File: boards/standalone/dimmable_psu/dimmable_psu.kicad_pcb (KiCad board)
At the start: 2 copper layers, 85 x 50 mm, 85 parts, among them J1 DIM_IN, J2 PWM_IN, J3 POWER, J4 POWER_OUT, Q1 2N7002, Q2 IRF540N, Q3 IRF540N, SW1 SW_DIP_SPLIT_x02, U1 LM324, U2 AP2205-ADJ, U3 MAX17651, U4 LMC7660, U5 TPS92640

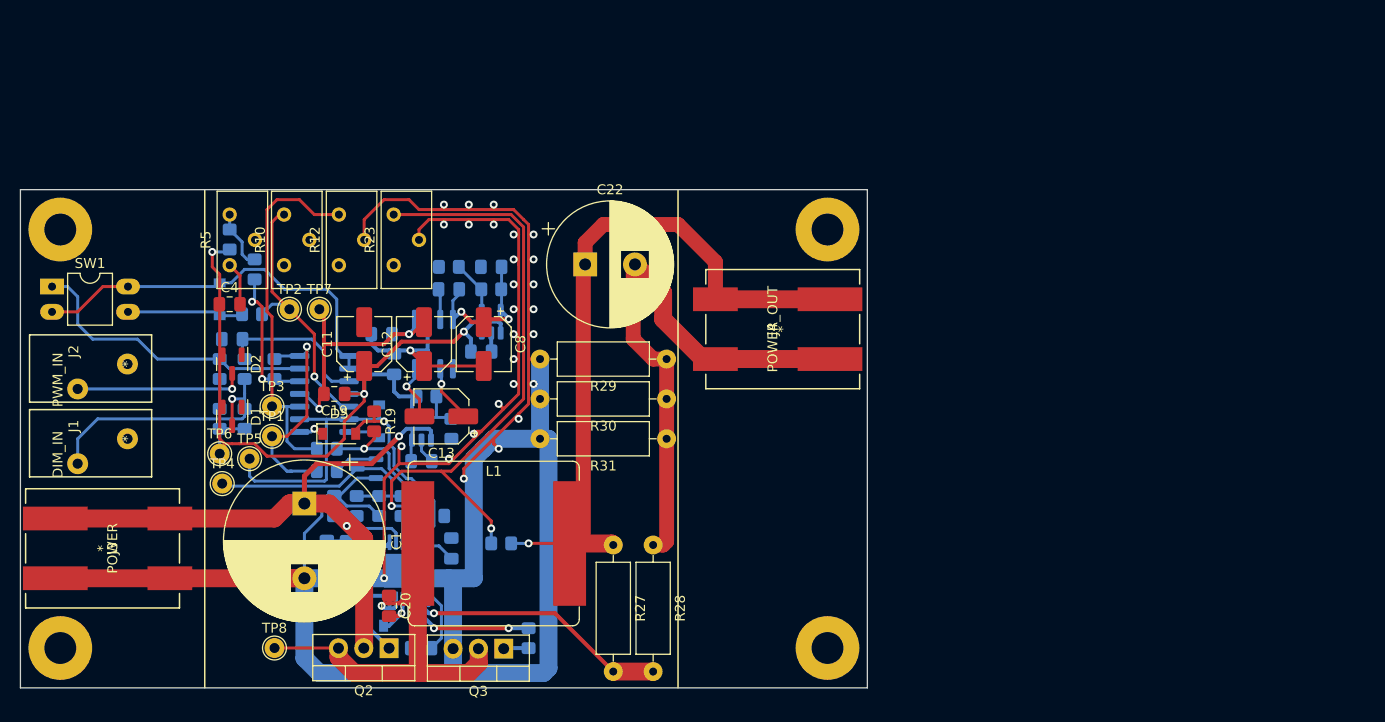
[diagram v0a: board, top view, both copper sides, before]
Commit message: add filled areas and make some cosmetic fixes
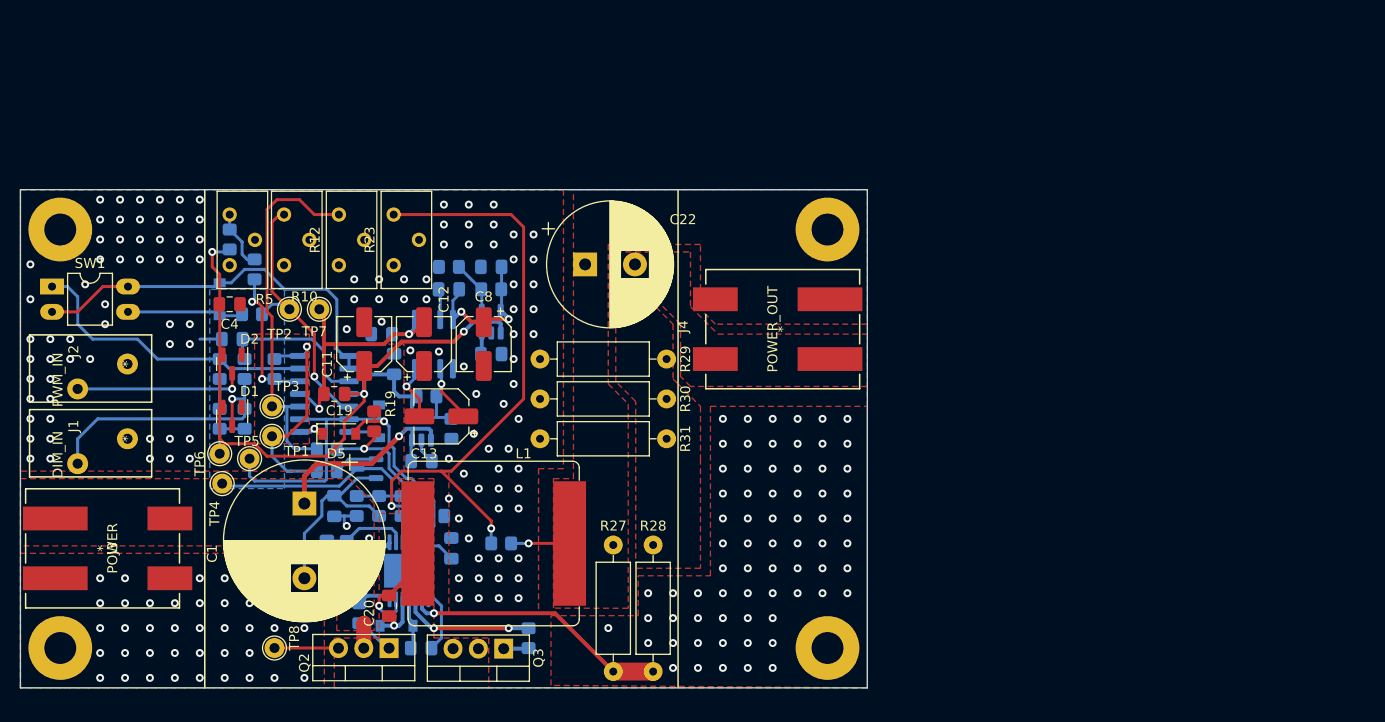
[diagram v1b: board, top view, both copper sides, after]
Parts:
- moved C6 1.03 mm to (47.2, 16.5)
- moved R25 0.50 mm to (34.0, 42.5)
- moved D6 0.35 mm to (37.8, 43.8)
- moved R11 0.05 mm to (30.8, 26.1)
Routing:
- net GND: track 316.9 -> 33.2 mm, vias 28 -> 228
- net /OUT+: track 71.8 -> 6.50 mm
- net /OUT-: track 56.6 -> 0.00 mm
- net VPP: track 75.6 -> 35.0 mm
- net /POWER_JUN: track 49.1 -> 18.1 mm
- net Net-(C20-Pad2): track 5.37 -> 6.43 mm
- net Net-(Q2-Pad1): track 3.54 -> 4.05 mm
- net Net-(R25-Pad1): track 2.91 -> 3.41 mm
- added copper zone on F.Cu, net /OUT+
- added copper zone on F.Cu, net /OUT-
- added copper zone on F.Cu, net /POWER_JUN
- added copper zone on B.Cu, net GND
- added copper zone on F.Cu, net GND
- added copper zone on F.Cu, net VPP

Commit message: replace LDOs with npns
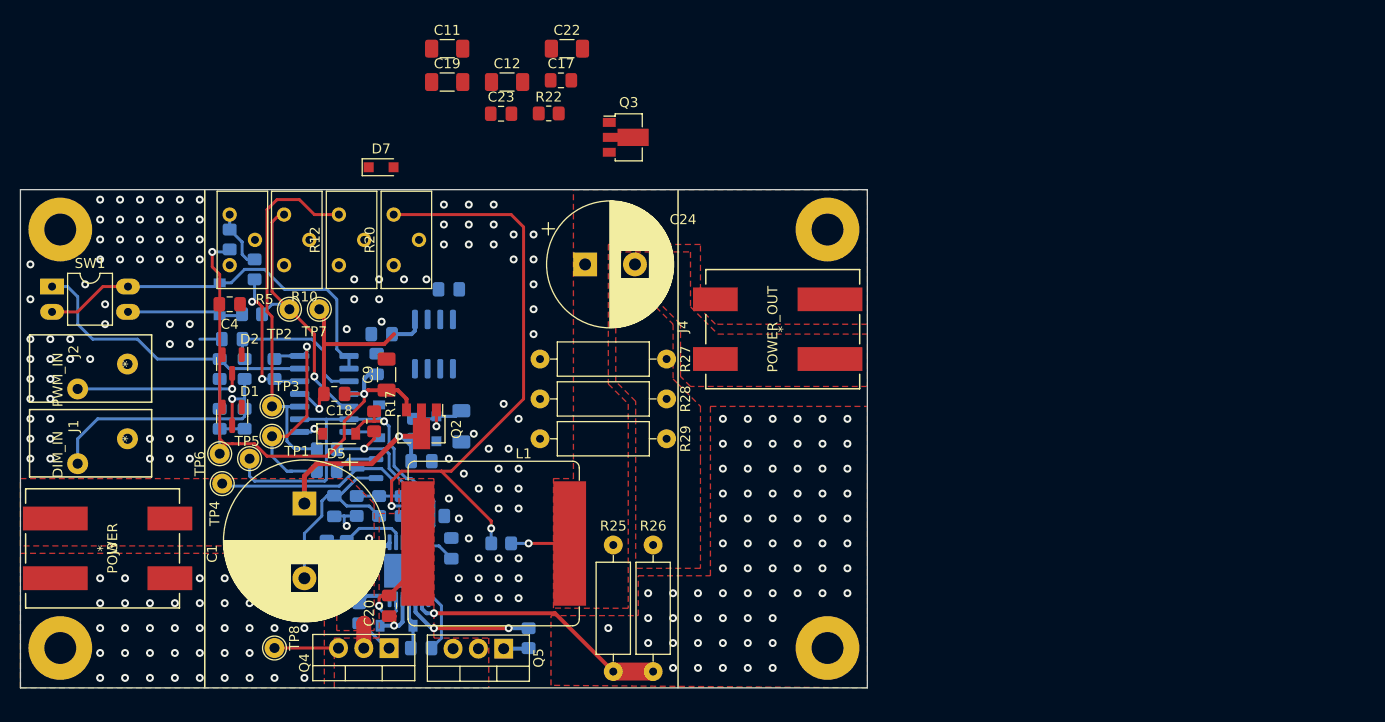
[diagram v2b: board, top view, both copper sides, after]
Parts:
- removed the C13 at (42.2, 22.8)
- removed the C6 at (47.2, 16.5)
- removed the C8 at (46.5, 15.5)
- removed the R16 at (47.2, 10.0)
- removed the R17 at (43.0, 7.75)
- removed the R20 at (40.8, 20.8)
- removed the R21 at (43.2, 24.0)
- removed the U2 at (47.2, 13.2)
- removed the U3 at (40.2, 24.0)
- added C17: 100n, Capacitor_SMD:C_0805_2012Metric_Pad1.18x1.45mm_HandSolder, F.Cu at (54.2, -11.0)
- added C19: 10µ, Capacitor_SMD:C_1206_3216Metric_Pad1.33x1.80mm_HandSolder, F.Cu at (42.8, -10.8)
- added C22: 10µ, Capacitor_SMD:C_1206_3216Metric_Pad1.33x1.80mm_HandSolder, F.Cu at (54.9, -14.2)
- added C23: 100n, Capacitor_SMD:C_0805_2012Metric_Pad1.18x1.45mm_HandSolder, F.Cu at (48.2, -7.62)
- added C7: 10µ, Capacitor_SMD:C_1206_3216Metric_Pad1.33x1.80mm_HandSolder, B.Cu at (44.2, 23.8)
- added D6: 15v, Diode_SMD:D_SOD-323_HandSoldering, B.Cu at (41.8, 24.0)
- added D7: 4v, Diode_SMD:D_SOD-323_HandSoldering, F.Cu at (36.2, -2.25)
- added Q2: BST52, Package_TO_SOT_SMD:SOT-89-3, F.Cu at (40.2, 23.8)
- added Q3: BST52, Package_TO_SOT_SMD:SOT-89-3, F.Cu at (60.8, -5.25)
- added R18: 4.7k, Resistor_SMD:R_0805_2012Metric_Pad1.20x1.40mm_HandSolder, B.Cu at (39.5, 24.0)
- added R22: 1.8k, Resistor_SMD:R_0805_2012Metric_Pad1.20x1.40mm_HandSolder, F.Cu at (53.0, -7.65)
- C11, C12: footprint Capacitor_SMD:CP_Elec_5x5.4 -> Capacitor_SMD:C_1206_3216Metric_Pad1.33x1.80mm_HandSolder
- C9: value 100n -> 10µ; footprint Capacitor_SMD:C_0805_2012Metric_Pad1.18x1.45mm_HandSolder -> Capacitor_SMD:C_1206_3216Metric_Pad1.33x1.80mm_HandSolder; moved to F.Cu
- moved C11 30.8 mm to (42.8, -14.2), turned to 0 degrees
- moved C12 27.6 mm to (48.8, -10.8), turned to 0 degrees
- moved C9 15.1 mm to (36.8, 18.6), turned to 90 degrees
- moved C10 1.75 mm to (35.8, 17.5)
- renumbered C14 to C10, C15 to C13, C16 to C14, C17 to C15, C18 to C16, C19 to C18, C22 to C24, C7 to C6, C10 to C8, D6 to D8, Q2 to Q4, Q3 to Q5, R18 to R16, R19 to R17, R22 to R19, R23 to R20, R24 to R21, R25 to R23, R26 to R24, R27 to R25, R28 to R26, R29 to R27, R30 to R28, R31 to R29, U4 to U2, U5 to U3
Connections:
- C11 pad 1: VDD -> GND
- C11 pad 2: GND -> -VSW
- C12 pad 1: GND -> Net-(C12-Pad1)
- C12 pad 2: -VSW -> Net-(C12-Pad2)
- C9 pad 1: /VNEGREF -> VDD
- U2 pad 2: Net-(C13-Pad1) (its old number) -> Net-(C12-Pad1)
- U2 pad 4: Net-(C13-Pad2) -> Net-(C12-Pad2)
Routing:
- net VDD: track 84.1 -> 58.7 mm, vias 3 -> 5
- net /VNEGREF: track 14.9 -> 0.00 mm, vias 2 -> 0
- net Net-(C7-Pad1): track 0.00 -> 7.74 mm, vias 0 -> 1
- net Net-(C13-Pad1) (its old number): track 5.73 -> 0.00 mm, vias 1 -> 0
- net Net-(C13-Pad2): track 5.66 -> 0.00 mm, vias 1 -> 0
- net Net-(R16-Pad2): track 5.32 -> 0.00 mm
- net Net-(R20-Pad2): track 4.11 -> 0.00 mm
- net -VSW: track 27.4 -> 24.0 mm, vias 2 -> 1
- net GND: track 33.2 -> 30.4 mm, vias 228 -> 212
- net Net-(C8-Pad2): track 2.60 -> 0.00 mm
- net Net-(C19-Pad1): vias 0 -> 2
- removed copper zone on B.Cu, net GND

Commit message: reorganise pcb
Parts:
- C12, C23: moved to B.Cu
- moved C17 35.0 mm to (36.2, 19.0), turned to 90 degrees
- moved C12 32.7 mm to (40.2, 20.8), turned to 180 degrees
- moved Q3 31.2 mm to (40.2, 18.2), turned to -90 degrees
- moved C22 29.5 mm to (43.2, 13.0), turned to 90 degrees
- moved C11 28.9 mm to (33.0, 13.0), turned to 90 degrees
- moved R22 28.1 mm to (44.2, 19.0), turned to 90 degrees
- moved C19 23.4 mm to (39.0, 12.2), turned to 180 degrees
- moved D7 16.9 mm to (38.8, 14.5), turned to 180 degrees
- moved C23 16.5 mm to (42.2, 7.75), turned to 180 degrees
- moved C9 3.76 mm to (33.0, 18.2)
- moved C18 1.68 mm to (32.2, 22.0)
- moved C8 0.79 mm to (42.2, 10.2)
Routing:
- net /VNEGREF: track 0.00 -> 15.1 mm, vias 0 -> 2
- net VDD: track 58.7 -> 71.1 mm, vias 5 -> 2
- net Net-(C19-Pad1): track 0.00 -> 9.09 mm, vias 2 -> 0
- net -VSW: track 24.0 -> 28.2 mm, vias 1 -> 2
- net Net-(C8-Pad2): track 0.00 -> 3.16 mm
- net Net-(C12-Pad2): track 0.00 -> 3.15 mm
- net Net-(C12-Pad1): track 0.00 -> 2.91 mm
- net GND: vias 212 -> 217

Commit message: restore zones
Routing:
- net GND: vias 217 -> 235
- added copper zone on B.Cu, net GND

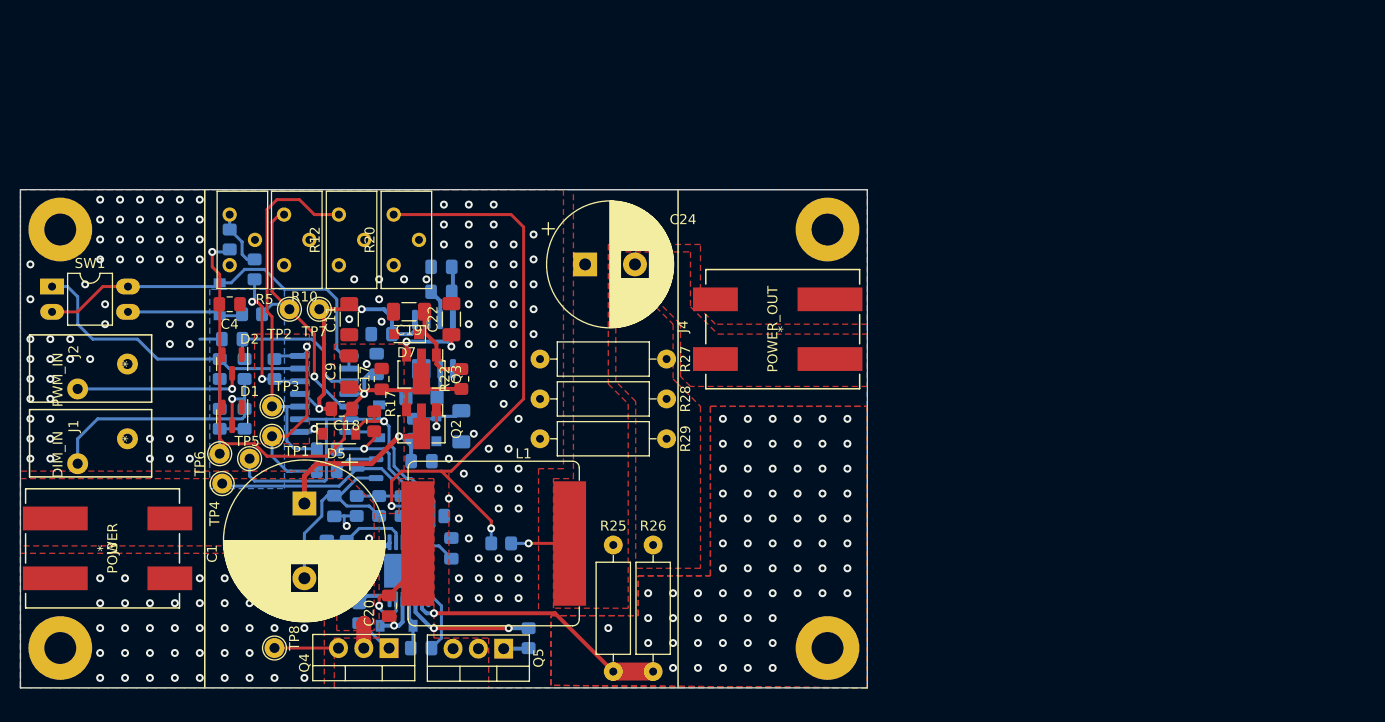
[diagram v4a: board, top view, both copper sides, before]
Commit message: use 1206 power resistors
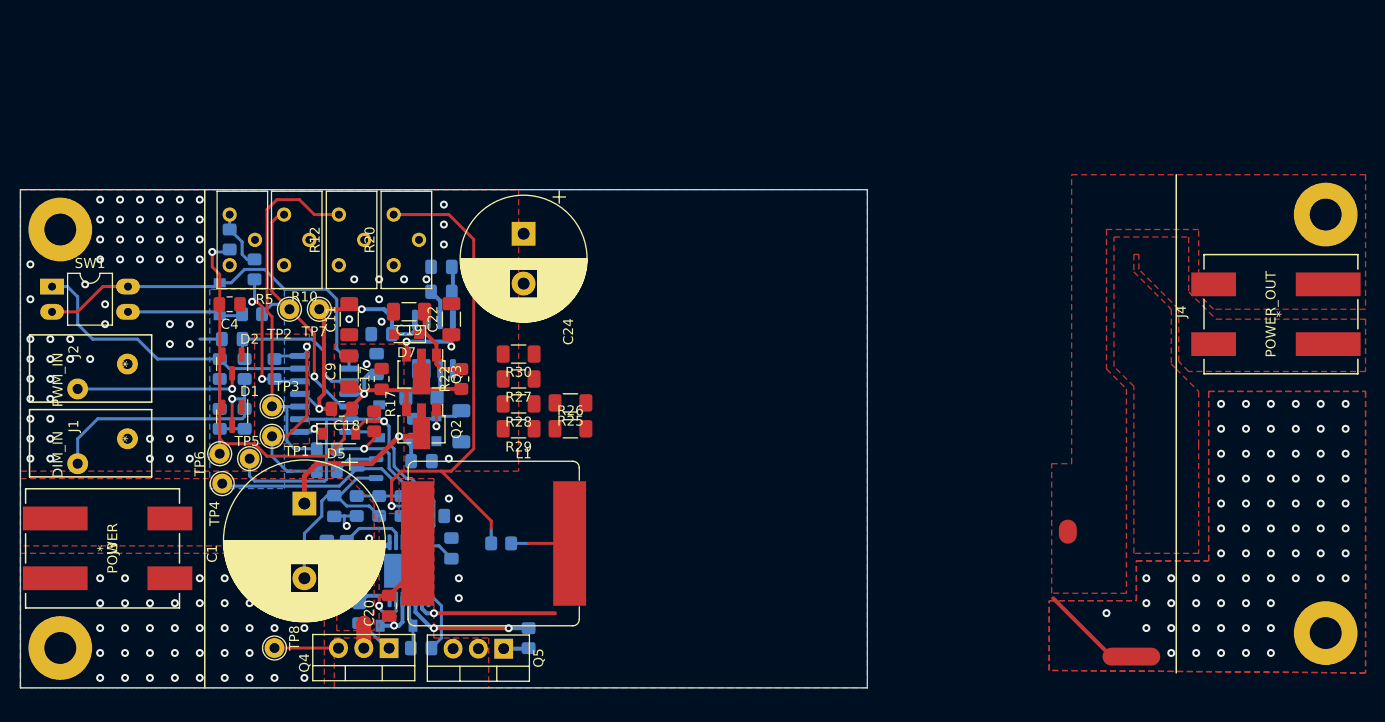
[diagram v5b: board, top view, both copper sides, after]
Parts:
- added R30: 0.18, Resistor_SMD:R_1206_3216Metric_Pad1.30x1.75mm_HandSolder, F.Cu at (50.0, 16.5)
- R25, R26: footprint Resistor_THT:R_Axial_DIN0309_L9.0mm_D3.2mm_P12.70mm_Horizontal -> Resistor_SMD:R_1206_3216Metric_Pad1.30x1.75mm_HandSolder
- R27, R28: value 0.2 -> 0.15; footprint Resistor_THT:R_Axial_DIN0309_L9.0mm_D3.2mm_P12.70mm_Horizontal -> Resistor_SMD:R_1206_3216Metric_Pad1.30x1.75mm_HandSolder
- R29: value 0.2 -> 0.18; footprint Resistor_THT:R_Axial_DIN0309_L9.0mm_D3.2mm_P12.70mm_Horizontal -> Resistor_SMD:R_1206_3216Metric_Pad1.30x1.75mm_HandSolder
- moved H2 50.0 mm to (131.0, 2.50)
- moved H3 50.0 mm to (131.0, 44.5)
- moved J4 50.0 mm to (126.5, 12.5)
- moved R27 15.0 mm to (50.0, 19.0)
- moved R25 14.9 mm to (55.2, 21.4), turned to 180 degrees
- moved R29 14.9 mm to (50.0, 24.0)
- moved R28 14.9 mm to (50.0, 21.5)
- moved R26 14.3 mm to (55.2, 24.0), turned to 0 degrees
- moved C24 6.90 mm to (50.5, 4.43), turned to -90 degrees
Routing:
- net /VOUT_SENSE: track 65.2 -> 57.4 mm, vias 2 -> 1
- net /OUT+: vias 1 -> 0
- net GND: vias 235 -> 181
